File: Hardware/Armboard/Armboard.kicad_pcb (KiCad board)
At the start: 2 copper layers, 118 parts, among them J1 Test_Point, SW1 SW_Push, SW2 SW_Push, SW3 SW_Push, SW4 SW_Push, SW5 SW_Push, SW6 SW_Push, U1 LM2576D2TR4, U2 TM4C129E_Launchpad

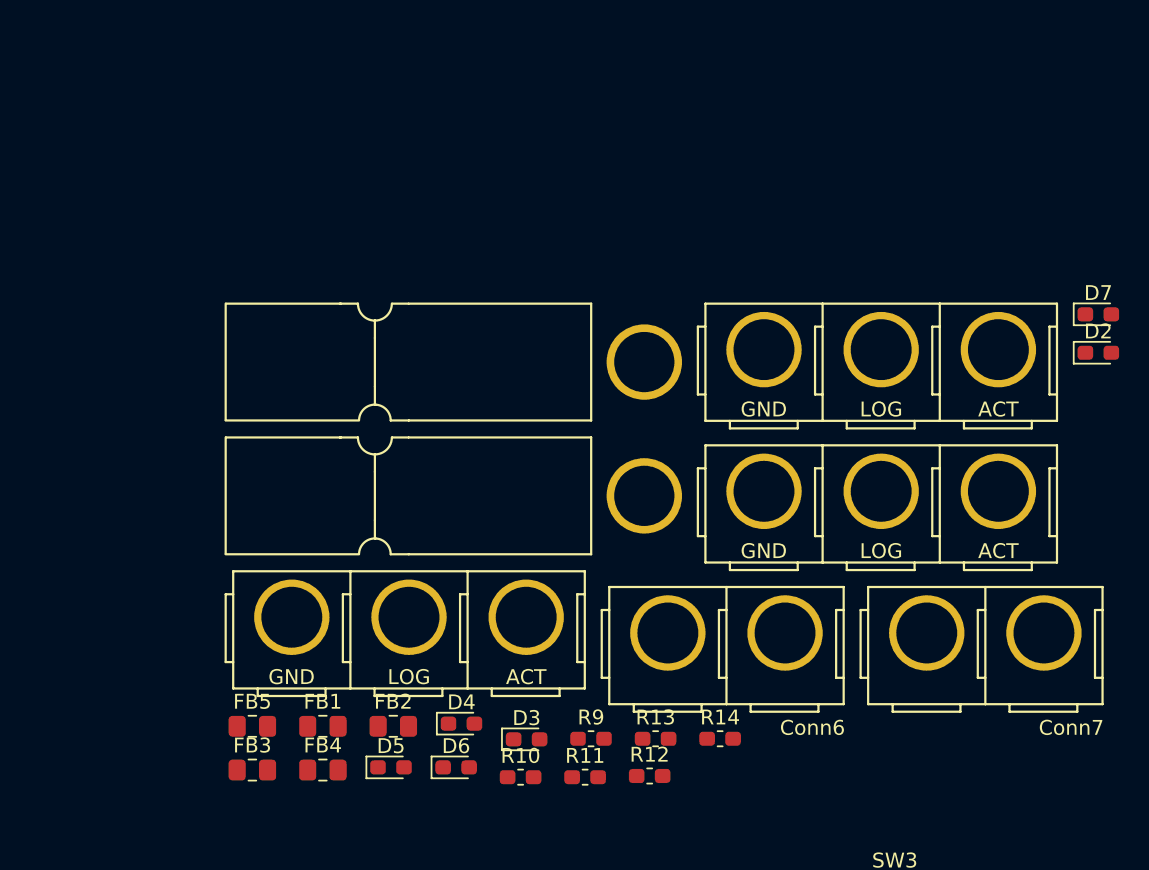
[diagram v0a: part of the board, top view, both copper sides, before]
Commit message: Fixed Andersons, made netlist, imported footprints to layout
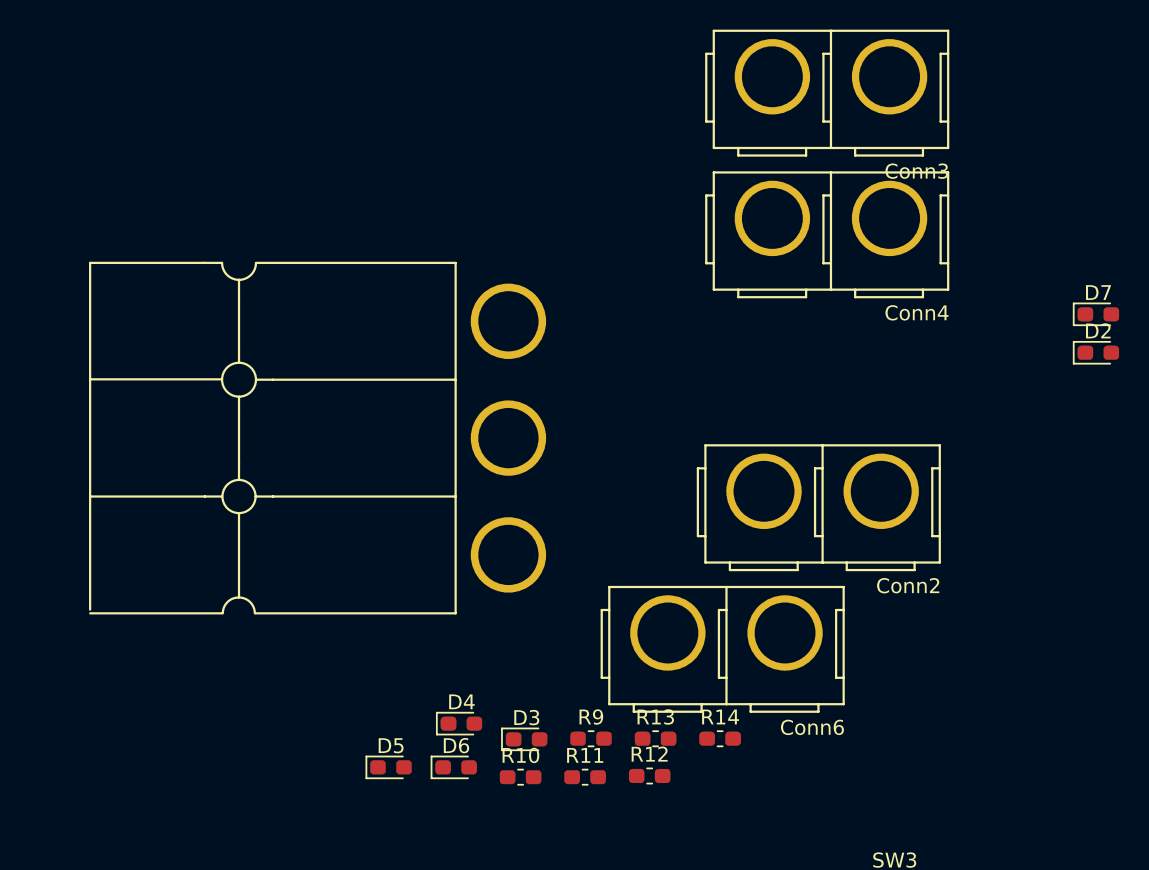
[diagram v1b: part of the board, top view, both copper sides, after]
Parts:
- removed Conn5: AndersonPP, MRDT_Connectors:Anderson_3_Vertical_Side_by_Side
- removed Conn7: AndersonPP, MRDT_Connectors:Anderson_2_Vertical_Sidy_by_Side
- removed FB1, FB2, FB3, FB4, FB5: Ferrite_Bead_Small, Capacitor_SMD:C_0805_2012Metric_Pad1.15x1.40mm_HandSolder
- Conn1: footprint MRDT_Connectors:Anderson_1_Horizontal -> MRDT_Connectors:Anderson_3_Horizontal_Side_by_Side
- Conn2: footprint MRDT_Connectors:Anderson_1_Horizontal -> MRDT_Connectors:Anderson_2_Vertical_Sidy_by_Side
- Conn3, Conn4: footprint MRDT_Connectors:Anderson_3_Vertical_Side_by_Side -> MRDT_Connectors:Anderson_2_Vertical_Sidy_by_Side
- moved Conn4 42.1 mm to (-33.0, 37.5)
- moved Conn3 18.4 mm to (-33.0, 27.9)
- moved Conn1 15.0 mm to (-50.8, 44.5)
- moved Conn2 11.8 mm to (-33.6, 55.9)
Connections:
- .1uF1 pad 1: +12VA -> /Power/12VA
- 10uF1 pad 1: +12VA -> /Power/12VA
- 10uF2 pad 1: +12VA -> /Power/12VA
- 10uF3 pad 1: +12VA -> /Power/12VA
- 10uF4 pad 1: +12VA -> /Power/12VA
- 47uF1 pad 1: +12VA -> /Power/12VA
- 47uF2 pad 1: +12VA -> /Power/12VA
- Conn1 pad 1: (no net) -> GND
- Conn3 pad 2: /Power/12V -> /Power/12VA
- Conn4 pad 2: /Power/12V -> /Power/12VA
- Conn6 pad 1: (no net) -> /H-Bridge/Gripper2
- Conn6 pad 2: Net-(Conn6-Pad2) -> /H-Bridge/Gripper1
- R11 pad 1: Net-(Conn2-Pad3) -> /Power/12VA
- R12 pad 1: Net-(Conn3-Pad3) -> /Power/12VA
- R13 pad 1: Net-(Conn4-Pad3) -> /Power/12VA
- R14 pad 1: Net-(Conn7-Pad2) -> /H-Bridge/Gripper2
- R9 pad 1: Net-(Conn6-Pad2) -> /H-Bridge/Gripper1

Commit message: Set board dimensions and started layout
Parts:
- SW5: moved to B.Cu
- moved U1 255.4 mm to (189.2, 94.1)
- moved 10uF1 243.6 mm to (190.9, 110.5)
- moved 10uF2 238.7 mm to (190.9, 113.0)
- moved 10uF3 238.4 mm to (190.9, 115.6)
- moved Conn1 238.4 mm to (171.4, 130.8), turned to 90 degrees
- moved .1uF1 234.6 mm to (190.9, 108.0)
- moved 10uF4 233.4 mm to (190.9, 118.1)
- moved 47uF2 230.6 mm to (174.9, 91.4)
- moved 47uF1 230.5 mm to (174.9, 99.1)
- moved Gripper_Motor1 222.4 mm to (105.8, 120.0)
- moved Conn2 206.4 mm to (158.7, 130.8), turned to 90 degrees
- moved Conn4 205.3 mm to (149.8, 130.8), turned to 90 degrees
- moved Conn3 202.1 mm to (141.0, 130.8), turned to 90 degrees
- moved Conn6 183.9 mm to (134.6, 122.9), turned to 270 degrees
- moved D8 8.72 mm to (-55.9, 115.9)
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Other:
- board outline added: 124.8 x 100.4 mm

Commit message: Added buckman and power leds to layout
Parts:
- moved J1 249.5 mm to (189.2, 86.6)
- moved D8 246.0 mm to (189.7, 101.3)
- moved C7 238.5 mm to (195.2, 106.7)
- moved L1 237.3 mm to (188.5, 96.4), turned to 270 degrees
- moved D6 234.0 mm to (179.3, 88.1)
- moved C8 233.4 mm to (189.3, 91.4)
- moved R10 230.0 mm to (179.4, 91.2)
- moved D5 207.1 mm to (145.5, 108.8), turned to 270 degrees
- moved D4 196.7 mm to (139.2, 108.9), turned to 270 degrees
- moved R13 191.0 mm to (145.5, 113.9), turned to 90 degrees
- moved D3 186.0 mm to (132.8, 108.9), turned to 270 degrees
- moved R12 184.6 mm to (139.2, 113.9), turned to 90 degrees
- moved R11 182.6 mm to (132.8, 113.9), turned to 90 degrees
- moved U2 125.6 mm to (-110.5, 41.9), turned to 180 degrees
- moved .1uF1 39.0 mm to (152.4, 113.9), turned to 90 degrees
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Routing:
- net /Power/12VA: track 0.00 -> 45.6 mm
- net /Power/12V: track 0.00 -> 32.3 mm
- net +3V3: track 0.00 -> 23.6 mm
- net Net-(D8-Pad1): track 0.00 -> 10.1 mm

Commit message: Added more components to layout
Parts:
- SW5: moved to F.Cu
- moved Conn10 388.2 mm to (183.0, 51.7)
- moved Conn11 388.2 mm to (183.0, 67.3)
- moved Conn12 384.5 mm to (166.6, 51.7)
- moved Conn9 384.5 mm to (166.6, 67.3)
- moved Conn13 380.8 mm to (150.2, 67.3)
- moved Conn8 380.8 mm to (150.2, 51.7)
- moved D29 333.3 mm to (176.5, 100.5), turned to 90 degrees
- moved D28 332.6 mm to (171.4, 100.5), turned to 90 degrees
- moved R35 321.4 mm to (176.5, 96.4), turned to 270 degrees
- moved D31 317.0 mm to (164.1, 100.4), turned to 90 degrees
- moved R34 312.1 mm to (171.4, 96.4), turned to 90 degrees
- moved D30 311.6 mm to (159.0, 100.4), turned to 90 degrees
- moved D33 308.8 mm to (151.4, 100.5), turned to 90 degrees
- moved R36 308.4 mm to (159.0, 96.4), turned to 90 degrees
- moved D32 308.2 mm to (146.3, 100.4), turned to 90 degrees
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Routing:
- net +3V3: track 23.6 -> 208.1 mm
- net /H-Bridge/Gripper2: track 0.00 -> 50.8 mm, vias 0 -> 2
- net /H-Bridge/Gripper1: track 0.00 -> 45.2 mm
- net Net-(Gripper_Motor1-Pad10): track 0.00 -> 34.4 mm
- net Net-(Gripper_Motor1-Pad9): track 0.00 -> 32.7 mm
- net GND: track 0.00 -> 30.5 mm
- net /Power/12VA: track 45.6 -> 76.0 mm
- net +12VA: track 0.00 -> 28.7 mm
- net Net-(Gripper_Motor1-Pad7): track 0.00 -> 19.0 mm
- net Net-(Gripper_Motor1-Pad6): track 0.00 -> 15.6 mm
- net Net-(Gripper_Motor1-Pad5): track 0.00 -> 12.1 mm
- net Net-(Gripper_Motor1-Pad8): track 0.00 -> 10.8 mm
- net Net-(Gripper_Motor1-Pad4): track 0.00 -> 8.65 mm
- net Motor_6: track 0.00 -> 7.95 mm
- net Motor_5: track 0.00 -> 7.95 mm
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
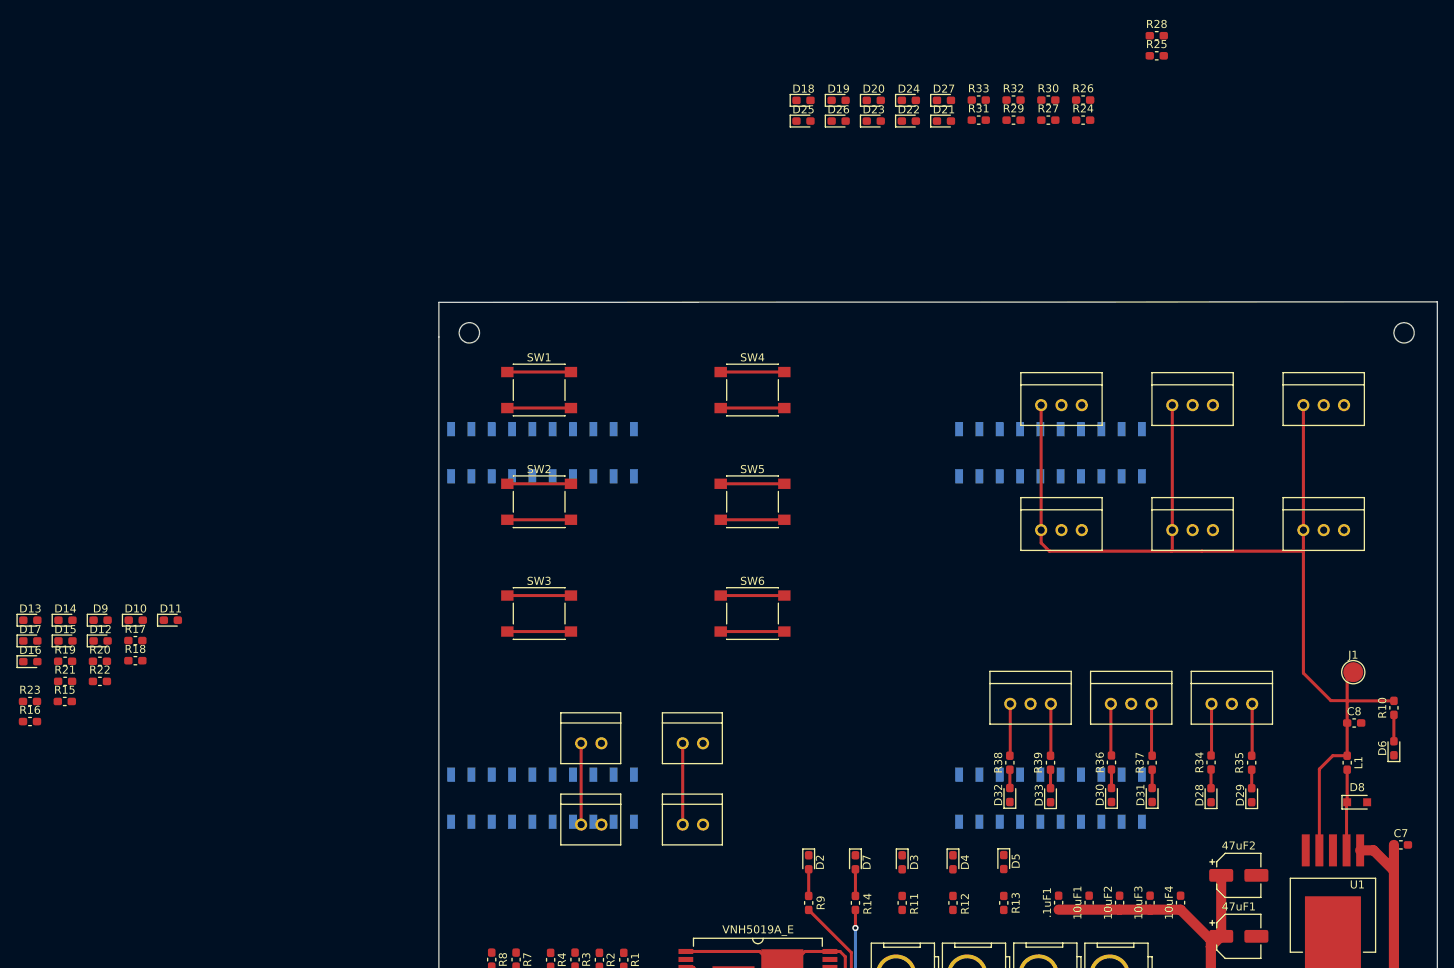
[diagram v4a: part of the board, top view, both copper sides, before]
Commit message: Finished general component layout
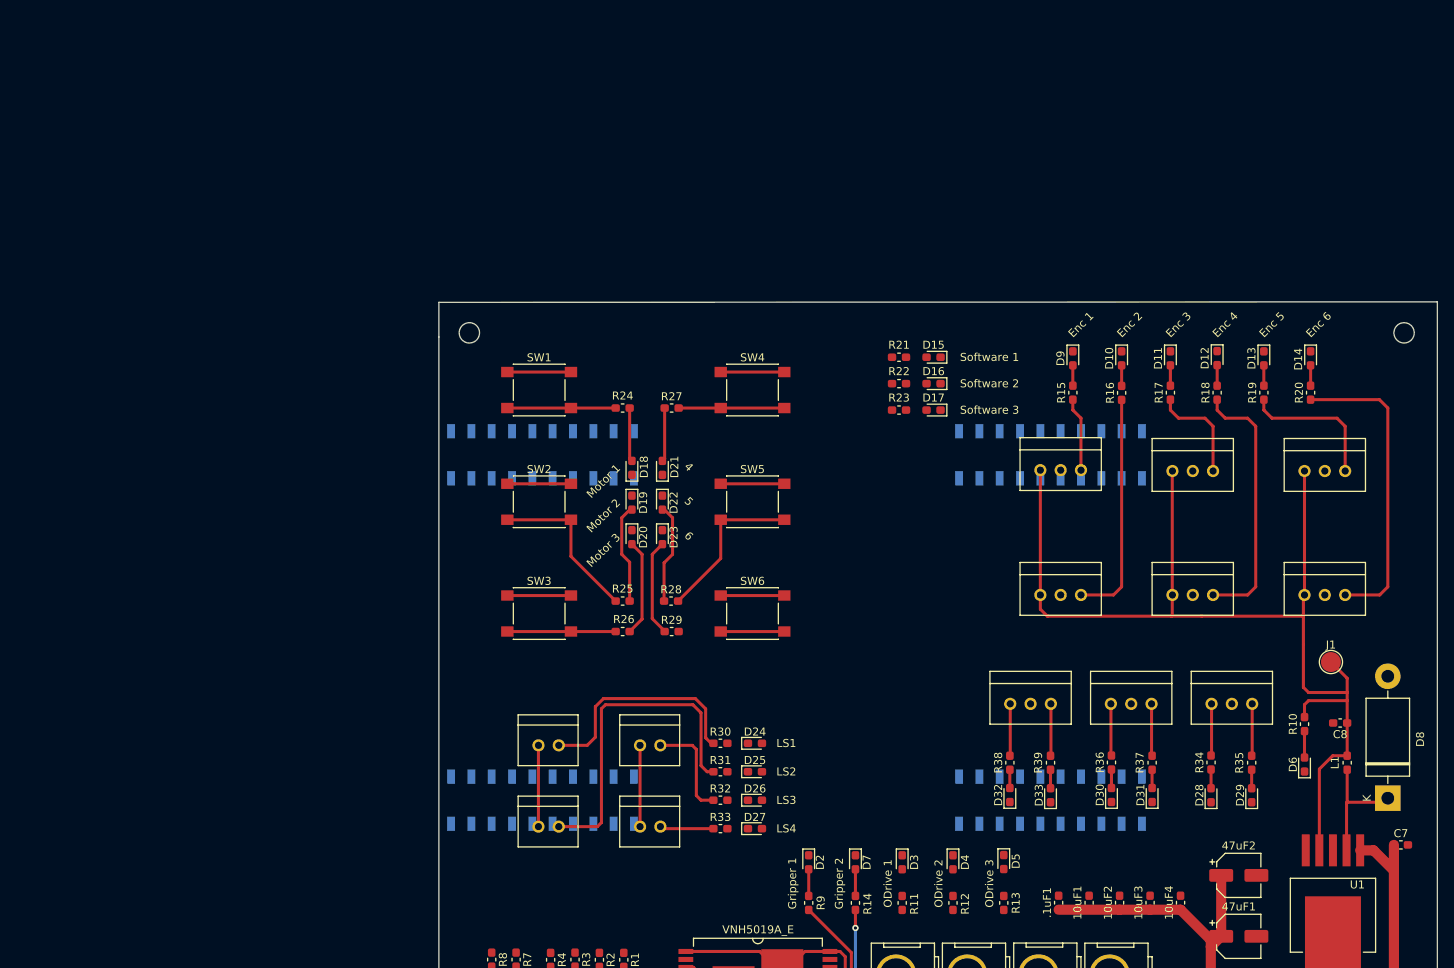
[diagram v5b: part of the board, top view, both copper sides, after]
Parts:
- D8: footprint Diode_SMD:D_SOD-323_HandSoldering -> Diode_THT:D_DO-201AD_P15.24mm_Horizontal
- moved D14 159.0 mm to (183.9, 45.9), turned to 270 degrees
- moved D13 157.6 mm to (178.1, 45.9), turned to 270 degrees
- moved R20 155.0 mm to (183.9, 50.2), turned to 90 degrees
- moved R19 153.6 mm to (178.1, 50.2), turned to 90 degrees
- moved D12 144.0 mm to (172.2, 45.8), turned to 270 degrees
- moved R16 142.5 mm to (160.3, 50.2), turned to 90 degrees
- moved R18 139.3 mm to (172.2, 50.2), turned to 90 degrees
- moved R17 133.0 mm to (166.4, 50.2), turned to 90 degrees
- moved R15 131.8 mm to (154.2, 50.2), turned to 90 degrees
- moved D11 129.2 mm to (166.4, 45.9), turned to 270 degrees
- moved D10 127.5 mm to (160.3, 45.9), turned to 270 degrees
- moved D9 125.9 mm to (154.2, 45.9), turned to 270 degrees
- moved D16 118.1 mm to (136.8, 49.0), turned to 180 degrees
- moved D17 116.5 mm to (136.8, 52.3), turned to 180 degrees
- moved R23 114.6 mm to (132.4, 52.3), turned to 180 degrees
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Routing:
- net LS_2: track 0.00 -> 41.3 mm
- net Enc_6_PWM: track 0.00 -> 38.2 mm
- net Enc_4_PWM: track 0.00 -> 32.8 mm
- net Enc_2_PWM: track 0.00 -> 28.9 mm
- net LS_1: track 0.00 -> 28.4 mm
- net Enc_5_PWM: track 0.00 -> 17.9 mm
- net Enc_3_PWM: track 0.00 -> 13.1 mm
- net LS_3: track 0.00 -> 12.9 mm
- net Net-(D22-Pad2): track 0.00 -> 12.5 mm
- net Net-(D19-Pad2): track 0.00 -> 12.5 mm
- net Motor_2: track 7.95 -> 20.4 mm
- net Motor_5: track 7.95 -> 20.3 mm
- net Net-(D23-Pad2): track 0.00 -> 12.2 mm
- net Net-(D20-Pad2): track 0.00 -> 12.1 mm
- net Enc_1_PWM: track 0.00 -> 9.23 mm
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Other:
- board text added: "4"
- board text added: "5"
- board text added: "6"
- board text added: "Enc 1"
- board text added: "Enc 2"
- board text added: "Enc 3"
- board text added: "Enc 4"
- board text added: "Enc 5"
- board text added: "Enc 6"
- board text added: "Gripper 1"
- board text added: "Gripper 2"
- board text added: "LS1"
- board text added: "LS2"
- board text added: "LS3"
- board text added: "LS4"
- board text added: "Motor 1"
- board text added: "Motor 2"
- board text added: "Motor 3"
- board text added: "ODrive 1"
- board text added: "ODrive 2"
- board text added: "ODrive 3"
- board text added: "Software 1"
- board text added: "Software 2"
- board text added: "Software 3"

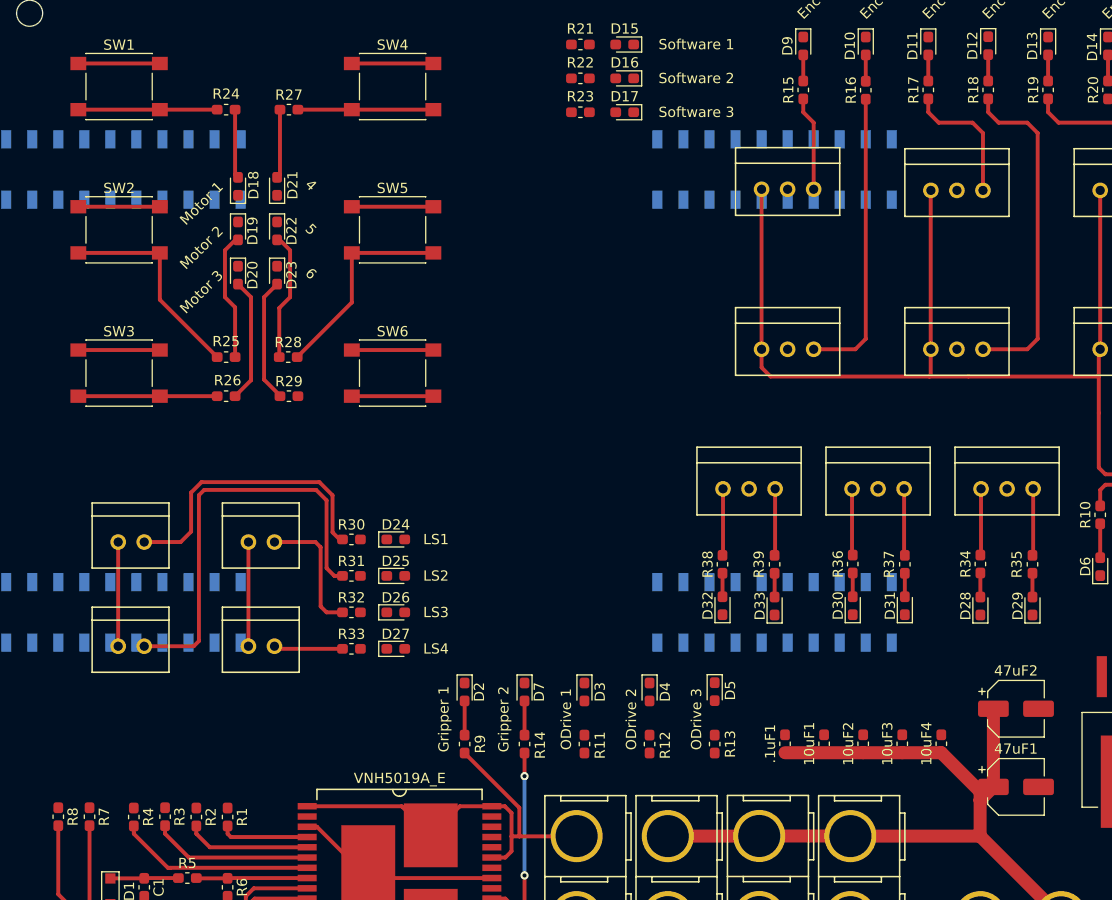
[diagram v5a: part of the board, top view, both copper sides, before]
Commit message: Made more connections to tiva
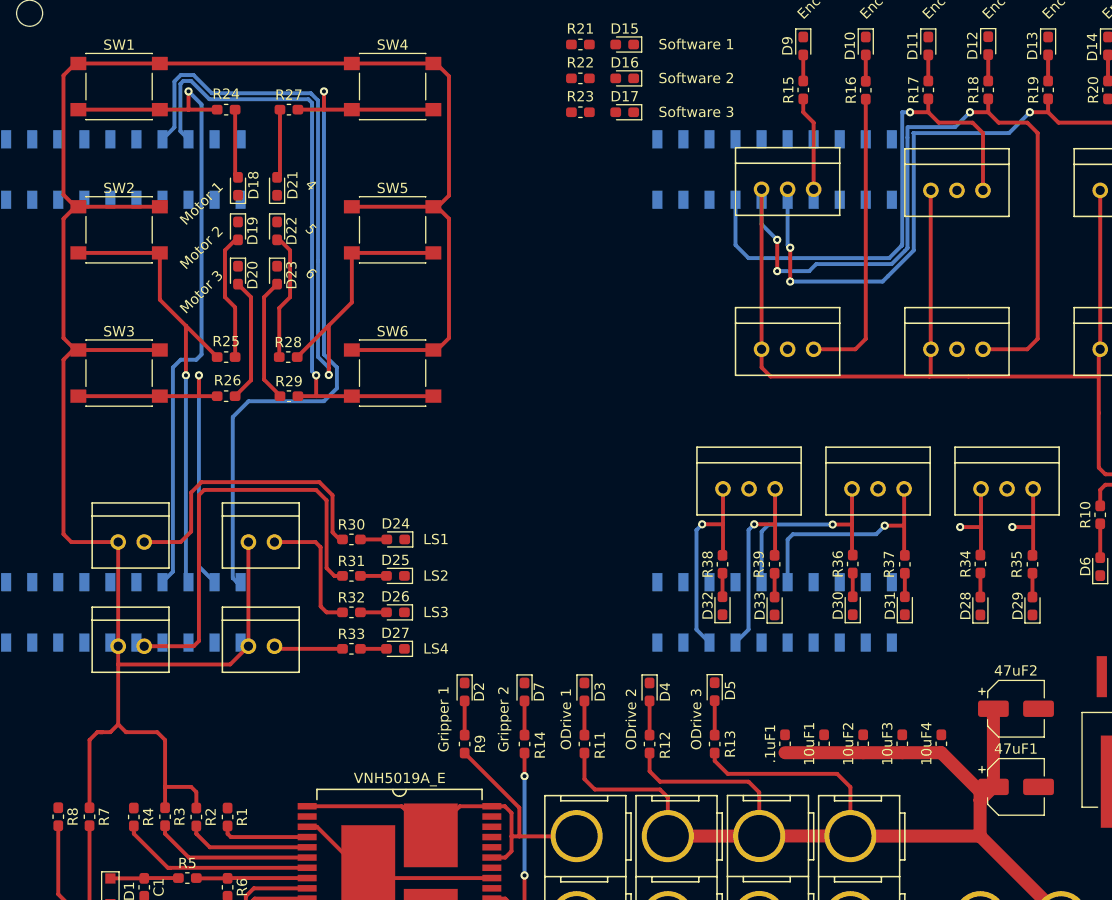
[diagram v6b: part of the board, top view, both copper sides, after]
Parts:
- turned D25 to 180 degrees
- turned D26 to 180 degrees
- turned D27 to 180 degrees
- turned D24 to 180 degrees
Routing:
- net +3V3: track 203.6 -> 356.8 mm
- net Motor_4: track 13.2 -> 72.4 mm, vias 0 -> 1
- net Motor_6: track 7.95 -> 61.5 mm, vias 0 -> 1
- net Motor_5: track 20.3 -> 73.8 mm, vias 0 -> 1
- net Motor_1: track 13.5 -> 66.2 mm, vias 0 -> 1
- net /Power/12VA: track 76.0 -> 128.6 mm
- net Enc_5_PWM: track 17.9 -> 64.6 mm, vias 0 -> 3
- net Enc_4_PWM: track 32.8 -> 74.1 mm, vias 0 -> 3
- net Enc_3_PWM: track 13.1 -> 50.3 mm, vias 0 -> 1
- net Motor_2: track 20.4 -> 45.5 mm, vias 0 -> 1
- net Motor_3: track 13.5 -> 36.4 mm, vias 0 -> 1
- net Tx_2_Tiva: track 6.51 -> 22.6 mm, vias 0 -> 1
- net Rx_3_Tiva: track 6.50 -> 20.8 mm, vias 0 -> 1
- net Tx_3_Tiva: track 6.50 -> 20.8 mm, vias 0 -> 1
- net Rx_2_Tiva: track 6.49 -> 20.5 mm, vias 0 -> 1
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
